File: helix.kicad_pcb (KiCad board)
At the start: 2 copper layers, 132 x 94 mm, 161 parts, among them J1 MJ-4PP-9, P3 OLED, Q1 2SC2712, Q2 2SC2712, SW1 SW_PUSH, SW10 SW_PUSH, SW11 SW_PUSH, SW12 SW_PUSH, SW13 SW_PUSH, SW14 SW_PUSH, SW15 SW_PUSH, SW16 SW_PUSH, SW17 SW_PUSH, SW18 SW_PUSH, SW19 SW_PUSH, SW2 SW_PUSH, SW20 SW_PUSH, SW21 SW_PUSH, SW22 SW_PUSH, SW23 SW_PUSH, SW24 SW_PUSH, SW25 SW_PUSH, SW26 SW_PUSH, SW27 SW_PUSH, SW28 SW_PUSH, SW29 SW_PUSH, SW3 SW_PUSH, SW30 SW_PUSH, SW31 SW_PUSH, SW32 SW_PUSH, SW33 Reset, SW34 SW_PUSH, SW35 SW_PUSH, SW36 SW_PUSH, SW37 SW_PUSH, SW38 SW_PUSH, SW39 SW_PUSH, SW4 SW_PUSH, SW40 SW_PUSH, SW41 SW_PUSH, SW42 SW_PUSH, SW43 SW_PUSH, SW44 SW_PUSH, SW45 SW_PUSH, SW46 SW_PUSH, SW47 SW_PUSH, SW48 SW_PUSH, SW49 SW_PUSH, SW5 SW_PUSH, SW50 SW_PUSH, SW51 SW_PUSH, SW52 SW_PUSH, SW53 SW_PUSH, SW54 SW_PUSH, SW55 SW_PUSH, SW56 SW_PUSH, SW57 SW_PUSH, SW58 SW_PUSH, SW59 SW_PUSH, SW6 SW_PUSH, SW60 SW_PUSH, SW61 SW_PUSH, SW62 SW_PUSH, SW63 SW_PUSH, SW64 SW_PUSH, SW65 SW_PUSH, SW7 SW_PUSH, SW8 SW_PUSH, SW9 SW_PUSH, U1 ProMicro, U34 74HC4051, U35 74HC4051, U36 AD8616, U37 AD8616, U38 ProMicro

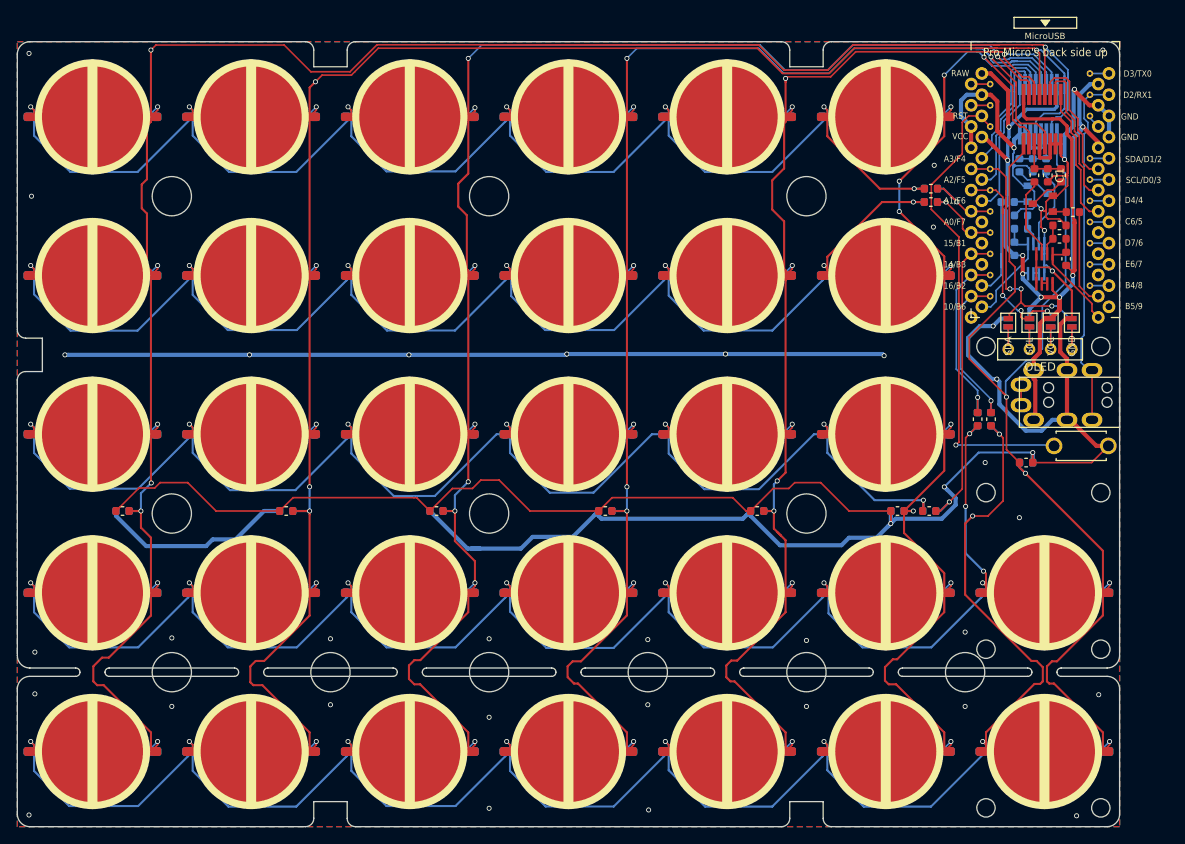
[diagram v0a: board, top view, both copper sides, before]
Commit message: ノイズ対策＆nizとvarmiloを同じリポジトリにした
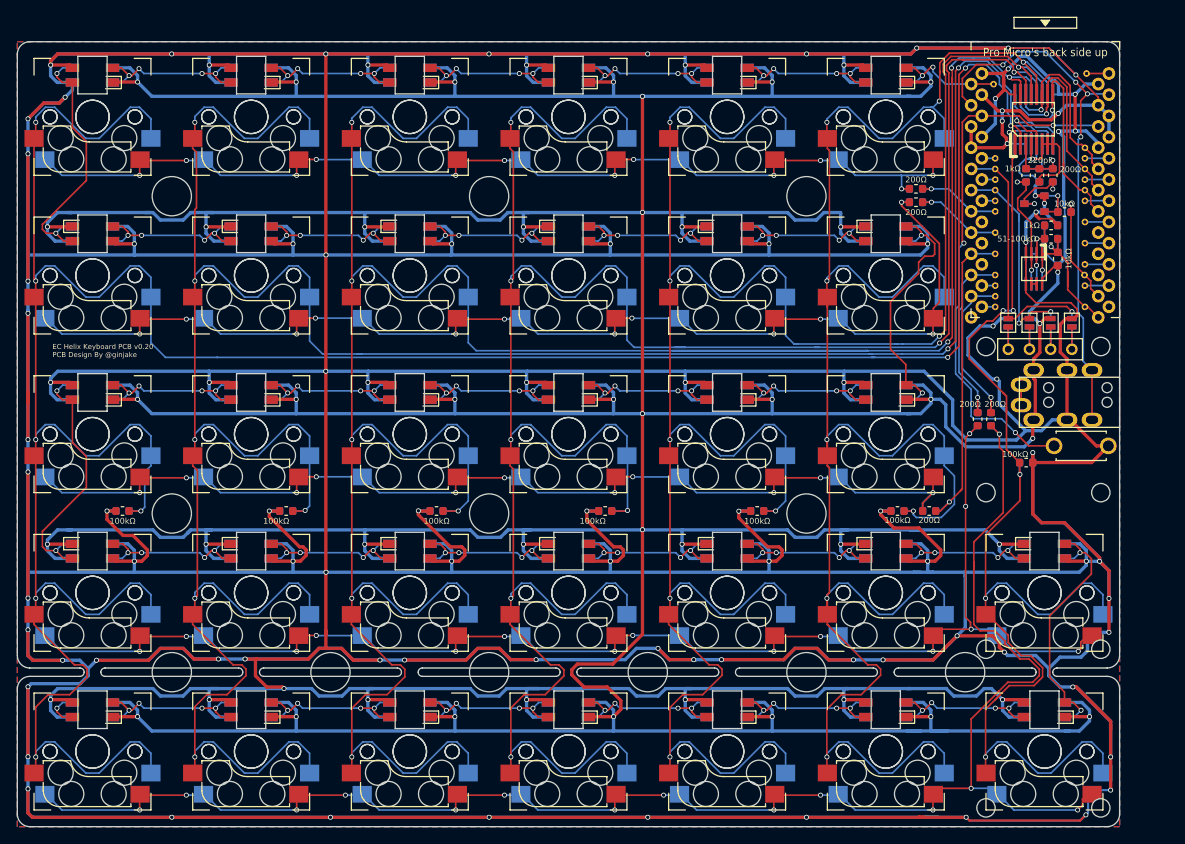
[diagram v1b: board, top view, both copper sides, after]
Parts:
- removed JP27, JP28: MountingHole_Pad, phi-kbd-library-master:THSmallest
- added JP35: MountingHole_Pad, phi-kbd-library-master:THSmallest, F.Cu at (200.1, 63.0)
- added JP36: MountingHole_Pad, phi-kbd-library-master:THSmallest, F.Cu at (210.8, 56.7)
- added JP37: MountingHole_Pad, phi-kbd-library-master:THSmallest, F.Cu at (210.8, 59.2)
- added JP38: MountingHole_Pad, phi-kbd-library-master:THSmallest, F.Cu at (210.8, 61.8)
- added JP39: MountingHole_Pad, phi-kbd-library-master:THSmallest, F.Cu at (200.1, 73.2)
- added JP40: MountingHole_Pad, phi-kbd-library-master:THSmallest, F.Cu at (200.1, 75.8)
- added JP41: MountingHole_Pad, phi-kbd-library-master:THSmallest, F.Cu at (210.8, 71.9)
- added JP42: MountingHole_Pad, phi-kbd-library-master:THSmallest, F.Cu at (210.8, 75.8)
- added L1: SK6812MINI, ec_helix:SK6812MINI_narrow-irreversible2, F.Cu at (92.0, 48.0)
- added L10: SK6812MINI, ec_helix:SK6812MINI_narrow-irreversible2, F.Cu at (149.0, 67.0)
- added L11: SK6812MINI, ec_helix:SK6812MINI_narrow-irreversible2, F.Cu at (168.0, 67.0)
- added L12: SK6812MINI, ec_helix:SK6812MINI_narrow-irreversible2, F.Cu at (187.0, 67.0)
- added L13: SK6812MINI, ec_helix:SK6812MINI_narrow-irreversible2, F.Cu at (92.0, 86.0)
- added L14: SK6812MINI, ec_helix:SK6812MINI_narrow-irreversible2, F.Cu at (111.0, 86.0)
- added L15: SK6812MINI, ec_helix:SK6812MINI_narrow-irreversible2, F.Cu at (130.0, 86.0)
- added L16: SK6812MINI, ec_helix:SK6812MINI_narrow-irreversible2, F.Cu at (149.0, 86.0)
- added L17: SK6812MINI, ec_helix:SK6812MINI_narrow-irreversible2, F.Cu at (168.0, 86.0)
- added L18: SK6812MINI, ec_helix:SK6812MINI_narrow-irreversible2, F.Cu at (187.0, 86.0)
- added L19: SK6812MINI, ec_helix:SK6812MINI_narrow-irreversible2, F.Cu at (92.0, 105.0)
- added L2: SK6812MINI, ec_helix:SK6812MINI_narrow-irreversible2, F.Cu at (111.0, 48.0)
- added L20: SK6812MINI, ec_helix:SK6812MINI_narrow-irreversible2, F.Cu at (111.0, 105.0)
- added L21: SK6812MINI, ec_helix:SK6812MINI_narrow-irreversible2, F.Cu at (130.0, 105.0)
- added L22: SK6812MINI, ec_helix:SK6812MINI_narrow-irreversible2, F.Cu at (149.0, 105.0)
- added L23: SK6812MINI, ec_helix:SK6812MINI_narrow-irreversible2, F.Cu at (168.0, 105.0)
- added L24: SK6812MINI, ec_helix:SK6812MINI_narrow-irreversible2, F.Cu at (187.0, 105.0)
- added L25: SK6812MINI, ec_helix:SK6812MINI_narrow-irreversible2, F.Cu at (206.0, 105.0)
- added L26: SK6812MINI, ec_helix:SK6812MINI_narrow-irreversible2, F.Cu at (92.0, 124.0)
- added L27: SK6812MINI, ec_helix:SK6812MINI_narrow-irreversible2, F.Cu at (111.0, 124.0)
- added L28: SK6812MINI, ec_helix:SK6812MINI_narrow-irreversible2, F.Cu at (130.0, 124.0)
- added L29: SK6812MINI, ec_helix:SK6812MINI_narrow-irreversible2, F.Cu at (149.0, 124.0)
- added L3: SK6812MINI, ec_helix:SK6812MINI_narrow-irreversible2, F.Cu at (130.0, 48.0)
- added L30: SK6812MINI, ec_helix:SK6812MINI_narrow-irreversible2, F.Cu at (168.0, 124.0)
- added L31: SK6812MINI, ec_helix:SK6812MINI_narrow-irreversible2, F.Cu at (187.0, 124.0)
- added L32: SK6812MINI, ec_helix:SK6812MINI_narrow-irreversible2, F.Cu at (206.0, 124.0)
- added L4: SK6812MINI, ec_helix:SK6812MINI_narrow-irreversible2, F.Cu at (149.0, 48.0)
- added L5: SK6812MINI, ec_helix:SK6812MINI_narrow-irreversible2, F.Cu at (168.0, 48.0)
- added L6: SK6812MINI, ec_helix:SK6812MINI_narrow-irreversible2, F.Cu at (187.0, 48.0)
- added L7: SK6812MINI, ec_helix:SK6812MINI_narrow-irreversible2, F.Cu at (92.0, 67.0)
- added L8: SK6812MINI, ec_helix:SK6812MINI_narrow-irreversible2, F.Cu at (111.0, 67.0)
- added L9: SK6812MINI, ec_helix:SK6812MINI_narrow-irreversible2, F.Cu at (130.0, 67.0)
- R16, R22: value 51kΩ -> 51-100kΩ
- SW1, SW10, SW11, SW12, SW13, SW14, SW15, SW16, SW17, SW18, SW19, SW2, SW20, SW21, SW22, SW23, SW24, SW25, SW26, SW27, SW28, SW29, SW3, SW30, SW31, SW32, SW34, SW35, SW36, SW37, SW38, SW39, SW4, SW40, SW41, SW42, SW43, SW44, SW45, SW46, SW47, SW48, SW49, SW5, SW50, SW51, SW52, SW53, SW54, SW55, SW56, SW57, SW58, SW59, SW6, SW60, SW61, SW62, SW63, SW64, SW65, SW7, SW8, SW9: footprint ec_helix:niz -> ec_helix:MX_Hotswap-1.00u-irreversible
- moved JP22 13.7 mm to (200.1, 58.0)
- moved JP26 8.91 mm to (200.1, 60.5)
- moved R23 6.91 mm to (208.4, 64.4), turned to 180 degrees
- moved R19 5.34 mm to (207.6, 70.0)
- moved R21 4.18 mm to (207.0, 60.0)
- moved R24 3.79 mm to (206.8, 66.0), turned to 0 degrees
- moved R22 3.79 mm to (206.8, 67.6), turned to 0 degrees
- moved R20 2.68 mm to (203.8, 60.0)
- moved R32 1.80 mm to (190.6, 61.6)
- moved R1 1.78 mm to (190.6, 61.6)
- moved R2 1.78 mm to (190.6, 63.2)
- moved R33 1.78 mm to (190.6, 63.2)
- moved C2 1.44 mm to (205.4, 60.0)
- moved U35 1.29 mm to (204.8, 53.3)
- moved Q2 1.26 mm to (204.8, 63.4), turned to 270 degrees
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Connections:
- C1 pad 1: a_ -> a
- JP1 pad 1: col00 -> col00_
- JP12 pad 1: col03 -> col03_
- JP13 pad 1: col04 -> col04_
- JP2 pad 1: col01 -> col01_
- JP20 pad 1: /SDA -> /SDA_
- JP22 pad 1: data -> row0_
- JP23 pad 1: /SCL -> /SCL_
- JP25 pad 1: LED -> LED_
- JP26 pad 1: data -> row1_
- JP3 pad 1: col02 -> col02_
- Q2 pad 1: Net-(Q2-Pad1) -> Net-(Q1-Pad1)
- Q2 pad 3: Net-(Q2-Pad3) -> Net-(Q1-Pad3)
- R13 pad 2: adc_ -> adc
- R14 pad 1: a_ -> a
- R15 pad 1: a_ -> a
- R16 pad 2: adc_ -> adc
- R17 pad 1: charge_ -> charge
- R20 pad 2: Net-(R20-Pad2) -> Net-(R14-Pad2)
- R21 pad 2: Net-(Q2-Pad3) -> Net-(Q1-Pad3)
- R22 pad 1: Net-(R22-Pad1) -> Net-(R16-Pad1)
- R23 pad 2: Net-(Q2-Pad1) -> Net-(Q1-Pad1)
- R24 pad 1: Net-(R22-Pad1) -> Net-(R16-Pad1)
- U1 pad 1: LED -> LED_
- U1 pad 10: col03 -> col03_
- U1 pad 11: col04 -> col04_
- U1 pad 13: adc -> adc_
- U1 pad 14: charge -> charge_
- U1 pad 18: row2 -> row2_
- U1 pad 19: row1 -> row1_
- U1 pad 20: row0 -> row0_
- U1 pad 5: /SDA -> /SDA_
- U1 pad 6: /SCL -> /SCL_
- U1 pad 7: col00 -> col00_
- U1 pad 8: col01 -> col01_
- U1 pad 9: col02 -> col02_
- U34 pad 10: row1_ -> row1
- U34 pad 11: row0_ -> row0
- U34 pad 12: a3 -> a6
- U34 pad 13: a0 -> a1
- U34 pad 14: a1 -> a5
- U34 pad 2: a6 -> a3
- U34 pad 3: a_ -> a
- U34 pad 5: a5 -> a0
- U34 pad 9: row2_ -> row2
- U35 pad 1: a4 -> a0
- U35 pad 12: a6 -> a2
- U35 pad 14: a2 -> a1
- U35 pad 15: a1 -> a6
- U35 pad 5: a0 -> a4
- U36 pad 1: adc_ -> adc
- U37 pad 2: Net-(R22-Pad1) -> Net-(R16-Pad1)
- U37 pad 3: Net-(R20-Pad2) -> Net-(R14-Pad2)
- U38 pad 13: adc_ -> adc
- U38 pad 14: charge_ -> charge
- U38 pad 18: row2_ -> row2
- U38 pad 19: row1_ -> row1
- U38 pad 20: row0_ -> row0
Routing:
- net GND: track 482.2 -> 2048.5 mm, vias 42 -> 101
- net VCC: track 133.9 -> 999.6 mm, vias 8 -> 44
- net a2: track 193.4 -> 337.8 mm
- net a1: track 152.5 -> 277.3 mm, vias 9 -> 8
- net a0: track 220.7 -> 341.9 mm
- net a3: track 242.9 -> 359.0 mm
- net a5: track 184.0 -> 297.9 mm, vias 9 -> 8
- net a6: track 143.4 -> 240.0 mm, vias 10 -> 8
- net col0: track 163.0 -> 126.6 mm, vias 7 -> 12
- net col2: track 165.1 -> 128.7 mm, vias 7 -> 11
- net Net-(L12-Pad1): track 0.00 -> 31.8 mm, vias 0 -> 2
- net Net-(L13-Pad1): track 0.00 -> 31.6 mm, vias 0 -> 2
- net Net-(L1-Pad1): track 0.00 -> 31.6 mm, vias 0 -> 2
- net Net-(L25-Pad1): track 0.00 -> 31.0 mm, vias 0 -> 2
- net col3: track 196.7 -> 171.5 mm, vias 10 -> 15
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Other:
- outline, holes or cut-outs redrawn
- net class bold: clearance 0.2 -> 0
- board text added: "EC Helix Keyboard PCB v0.20 PCB Design By @ginjake"
